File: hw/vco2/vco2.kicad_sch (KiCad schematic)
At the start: 51 parts, among them U4 TL072HxD, U5 TL072HxD

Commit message: Dual VCO board
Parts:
- removed H2, H3, H4: MountingHole, MountingHole:MountingHole_3.5mm, symbol Mechanical:MountingHole
- added C19, C20, C22, C23: 100n, Capacitor_SMD:C_0603_1608Metric_Pad1.08x0.95mm_HandSolder, symbol Device:C
- added C21: 100n, Capacitor_SMD:C_0805_2012Metric_Pad1.18x1.45mm_HandSolder, symbol Device:C
- added D3, D4: LED wave out, LED_THT:LED_D3.0mm, symbol Device:LED
- added J_CV2, J_PULSE2, J_PWM2, J_SAW2, J_TRI2: TS, Connector_Audio:Jack_3.5mm_QingPu_WQP-PJ398SM_Vertical_CircularHoles, symbol Connector_Audio:AudioJack2_SwitchT
- added R39, R44, R52, R53, R54, R55: 10k, Resistor_SMD:R_0603_1608Metric_Pad0.98x0.95mm_HandSolder, symbol Device:R
- added R40: 20k, Resistor_SMD:R_0603_1608Metric_Pad0.98x0.95mm_HandSolder, symbol Device:R
- added R41, R60, R61, R62: 1k, Resistor_SMD:R_0603_1608Metric_Pad0.98x0.95mm_HandSolder, symbol Device:R
- added R42, R43, R46, R49, R50: 49k9, Resistor_SMD:R_0603_1608Metric_Pad0.98x0.95mm_HandSolder, symbol Device:R
- added R45: 250k, Resistor_SMD:R_0603_1608Metric_Pad0.98x0.95mm_HandSolder, symbol Device:R
- added R51: 32k, Resistor_SMD:R_0603_1608Metric_Pad0.98x0.95mm_HandSolder, symbol Device:R
- added R56, R57, R58, R59: 39k, Resistor_SMD:R_0603_1608Metric_Pad0.98x0.95mm_HandSolder, symbol Device:R
- added RV_PWM2, RV_RANGE2, RV_TUNE2: 20k, Pot:RV9012NO, symbol Device:R_Potentiometer
- added TP7: TestPoint_Alt, Holes:TP_0.9mm, symbol Connector:TestPoint_Alt
- added U7, U8: TL072HxD, Package_SO:SOIC-8_3.9x4.9mm_P1.27mm, symbol Amplifier_Operational:TL072
- H1: footprint MountingHole:MountingHole_3.5mm -> MountingHole:MountingHole_3.2mm_M3_Pad
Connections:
- net +12V: now also C19.1, C22.1, U7.8 (V+), U8.8 (V+)
- net +2V5: now also R39.2, R40.2, R51.2, RV_TUNE2.3
- net -12V: now also C20.2, C23.2, U7.4 (V-), U8.4 (V-)
- net GND: now also C19.2, C20.1, C22.2, C23.1, D3.1 (K), D4.2 (A), J_CV2.S, J_PULSE2.S, J_PWM2.S, J_SAW2.S, J_TRI2.S, R41.1, R49.1, RV_RANGE2.1, RV_TUNE2.1
- net OPREF: now also U7.3 (+), U7.5 (+), U8.3 (+), U8.5 (+)
- net at J_CV1.T, R14.1: now also J_CV2.TN
- net EXPO_FREQ renamed EXPO_FREQ1
- net HARD_SYNC renamed HARD_SYNC1
- net LIN_FREQ renamed LIN_FREQ1
- net PULSE_OUT renamed PULSE1
- net PWM_CTRL renamed PWM_CTRL1
- net SAW_OUT renamed SAW1
- net TRI_OUT renamed TRI1
- new net: D3.2 (A), D4.1 (K), R62.2
- new net: R59.1, R62.1, U8.7
- new net: J_TRI2.T, R61.1
- new net: R58.1, R61.2, U8.1
- new net: R55.1, R59.2, U8.6 (-)
- new net: R54.1, R58.2, U8.2 (-)
- new net: R44.1, RV_RANGE2.2
- new net: R39.1, RV_RANGE2.3
- new net: R56.1, R60.2, U7.1
- new net: R52.1, R56.2, U7.2 (-)
- new net: C21.2, J_PULSE2.T
- new net: R53.1, R57.2, U7.6 (-)
- new net: J_CV2.T, R46.1
- new net: R45.1, RV_TUNE2.2
- new net: R43.2, R49.2, R50.1
- new net: C21.1, R57.1, U7.7
- new net: J_PWM2.T, R43.1
- new net: R40.1, RV_PWM2.1
- new net: R42.1, RV_PWM2.2
- new net: R41.2, RV_PWM2.3
- new net: J_SAW2.T, R60.1
- new net EXPO_FREQ2: R44.2, R45.2, R46.2, R51.1, TP7.1
- new net PULSE2: R53.2
- new net PWM_CTRL2: R42.2, R50.2
- new net SAW2: R52.2
- new net TRI2: R54.2, R55.2
- no-connect marks 3 -> 6
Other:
- added sheet Oscillator 2 (osc1.kicad_sch)
- sheet Oscillator 1 ports: added EXPO_FREQ, HARD_SYNC, LIN_FREQ, PULSE, PWM_CTRL, SAW, TRI; removed none
- note added: "INPUT 1"
- note added: "INPUT 2"
- note added: "OUTPUT 1"
- note added: "OUTPUT 2"
- moved on the sheet: C10, C11, C12, C14, C15, C16, C9, D1, D2, J_CV1, J_FM1, J_PULSE1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

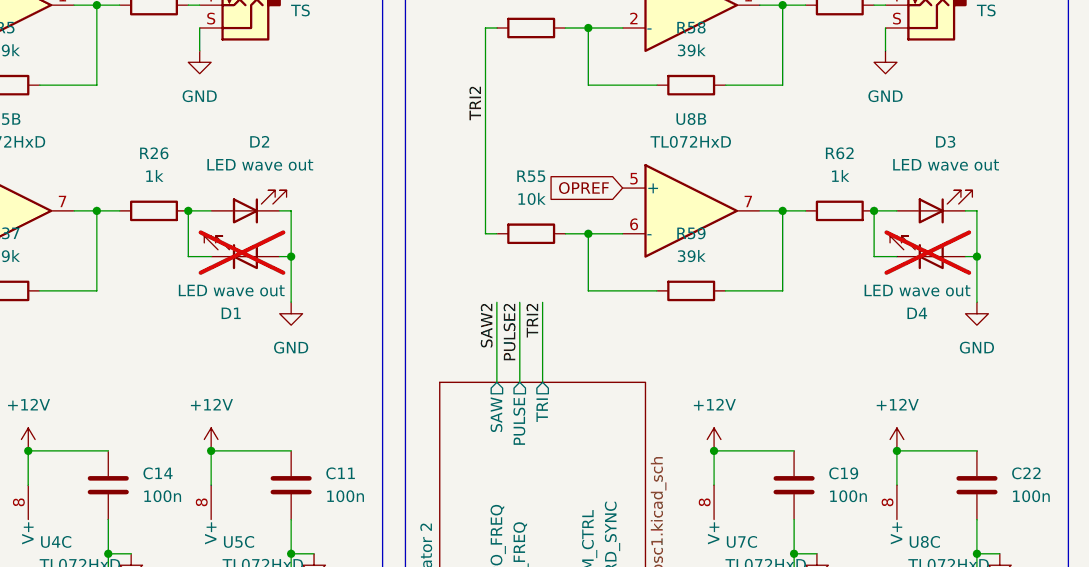
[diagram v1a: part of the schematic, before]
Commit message: Layout VCO2 board
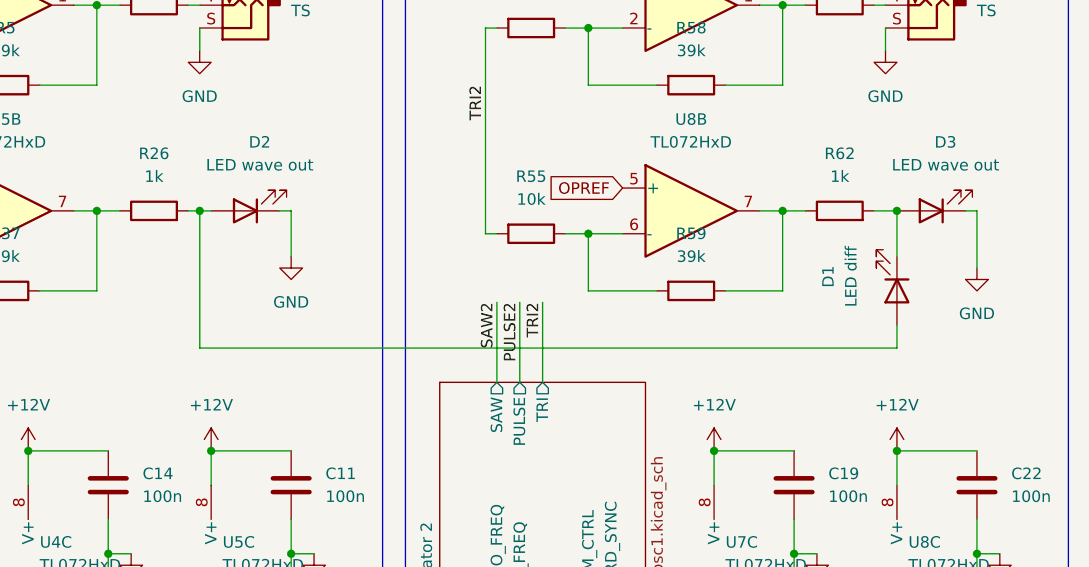
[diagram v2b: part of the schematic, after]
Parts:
- removed D4: LED wave out, LED_THT:LED_D3.0mm, symbol Device:LED
- D1: value LED wave out -> LED diff; now fitted
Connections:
- net GND: no longer D1.2 (A)
- net at D3.2 (A), R62.2: now also D1.1 (K)
- net at D2.2 (A), R26.2: now also D1.2 (A); no longer D1.1 (K)

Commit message: Place components
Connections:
- no-connect marks 6 -> 12
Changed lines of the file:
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@@
+	)
+	(no_connect
+		(at 261.62 29.21)
+	)
+	(no_connect
+		(at 185.42 29.21)
 	)
 	(no_connect
 		(at 31.75 102.87)
+	)
+	(no_connect
+		(at 185.42 53.34)
 	)
 	(no_connect
@@
 	)
 	(no_connect
+		(at 185.42 76.2)
+	)
+	(no_connect
 		(at 90.17 179.07)
+	)
+	(no_connect
+		(at 261.62 76.2)
 	)
 	(no_connect
@@
 	)
 	(no_connect
+		(at 261.62 53.34)
+	)
+	(no_connect

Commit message: Layout board
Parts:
- added H2, H3: MountingHole, Holes:MountingHole_3.2mm_M3_Pad, symbol Mechanical:MountingHole
- H1: footprint MountingHole:MountingHole_3.2mm_M3_Pad -> Holes:MountingHole_3.2mm_M3_Pad
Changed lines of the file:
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@@
 			)
 		)
-		(property "Footprint" "MountingHole:MountingHole_3.2mm_M3_Pad"
+		(property "Footprint" "Holes:MountingHole_3.2mm_M3_Pad"
 			(at 160.02 180.34 0)
 			(effects
@@
 	)
 	(symbol
+		(lib_id "Mechanical:MountingHole")
+		(at 160.02 170.18 0)
+		(unit 1)
+		(exclude_from_sim no)
+		(in_bom no)
+		(on_board yes)
+		(dnp no)
+		(fields_autoplaced yes)
+		(property "Reference" "H3"
+			(at 162.56 168.9099 0)
+			(effects
+				(font
+					(size 1.27 1.27)
+				)
+				(justify left)
+			)
+		)
+		(property "Value" "MountingHole"
+			(at 162.56 171.4499 0)
+			(effects
+				(font
+					(size 1.27 1.27)
+				)
+				(justify left)
+			)
+		)
+		(property "Footprint" "Holes:MountingHole_3.2mm_M3_Pad"
+			(at 160.02 170.18 0)
+			(effects
+				(font
+					(size 1.27 1.27)
+				)
+				(hide yes)
+			)
+		)
+		(property "Datasheet" "~"
+			(at 160.02 170.18 0)
+			(effects
+				(font
+					(size 1.27 1.27)
+				)
+				(hide yes)
+			)
+		)
+		(property "Description" "Mounting Hole without connection"
+			(at 160.02 170.18 0)
+			(effects
+				(font
+					(size 1.27 1.27)
+				)
+				(hide yes)
+			)
+		)
+		(instances
+			(project "vco2"
+				(path "/307302bf-1f04-498b-81c7-0944a093f10d"
+					(reference "H3")
+					(unit 1)
+				)
+			)
+		)
+	)
+	(symbol
 		(lib_id "Device:R")
 		(at 104.14 34.29 90)
@@
 					(unit 1)
 				)
+			)
+		)
+	)
+	(symbol
+		(lib_id "Mechanical:MountingHole")
+		(at 160.02 175.26 0)
+		(unit 1)
+		(exclude_from_sim no)
+		(in_bom no)
+		(on_board yes)
+		(dnp no)
+		(fields_autoplaced yes)
+		(property "Reference" "H2"
+			(at 162.56 173.9899 0)
+			(effects
+				(font
+					(size 1.27 1.27)
+				)
+				(justify left)
+			)
+		)
+		(property "Value" "MountingHole"
+			(at 162.56 176.5299 0)
+			(effects
+				(font
+					(size 1.27 1.27)
+				)
+				(justify left)
+			)
+		)
+		(property "Footprint" "Holes:MountingHole_3.2mm_M3_Pad"
+			(at 160.02 175.26 0)
+			(effects
+				(font
+					(size 1.27 1.27)
+				)
+				(hide yes)
+			)
+		)
+		(property "Datasheet" "~"
+			(at 160.02 175.26 0)
+			(effects
+				(font
+					(size 1.27 1.27)
+				)
+				(hide yes)
+			)
+		)
+		(property "Description" "Mounting Hole without connection"
+			(at 160.02 175.26 0)
+			(effects
+				(font
+					(size 1.27 1.27)
+				)
+				(hide yes)
+			)
+		)
+		(instances
+			(project "vco2"
+				(path "/307302bf-1f04-498b-81c7-0944a093f10d"
+					(reference "H2")
+					(unit 1)
+				)

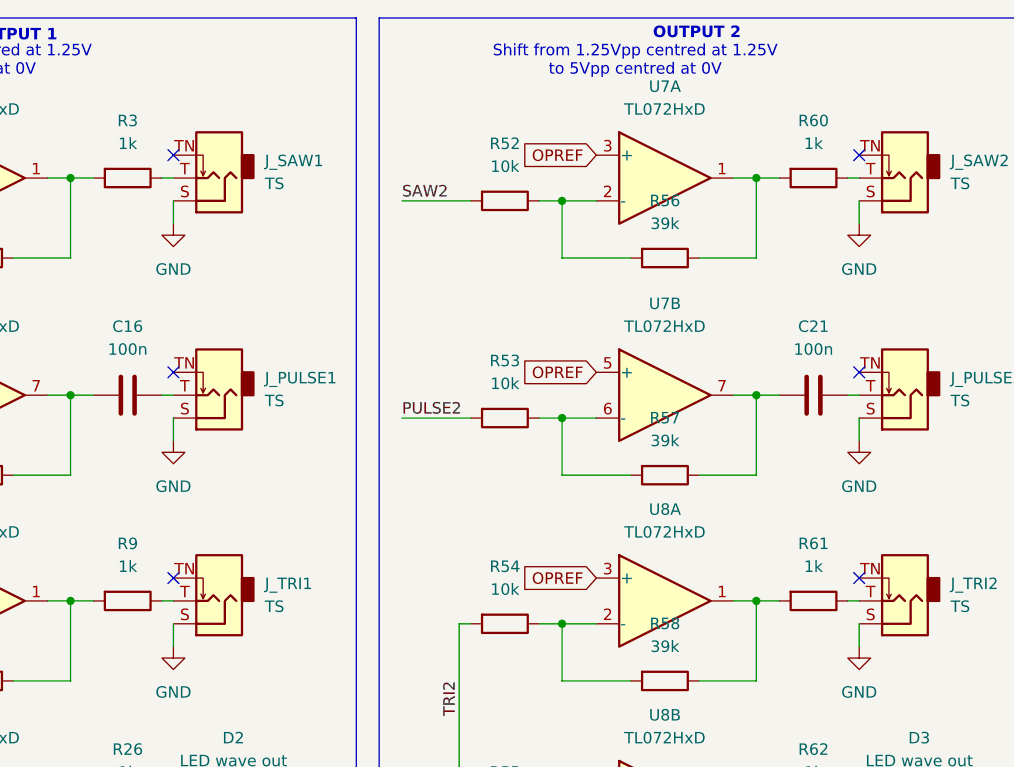
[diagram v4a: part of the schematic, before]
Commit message: Add normalisation on outputs
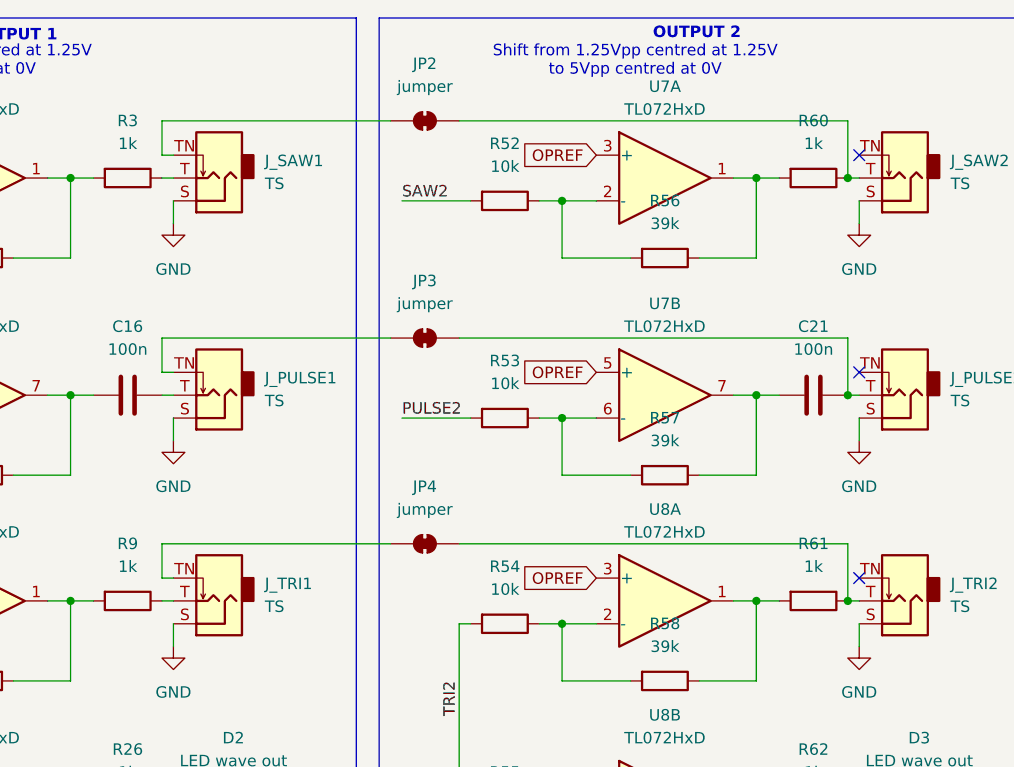
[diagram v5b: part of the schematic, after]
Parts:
- added JP2, JP4: jumper, Jumper:SolderJumper-2_P1.3mm_Bridged2Bar_Pad1.0x1.5mm, symbol Jumper:SolderJumper_2_Bridged
- added JP3: jumper, Jumper:SolderJumper-2_P1.3mm_Open_Pad1.0x1.5mm, symbol Jumper:SolderJumper_2_Bridged
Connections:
- net at J_TRI2.T, R61.1: now also JP4.1 (A)
- net at J_TRI1.TN: now also JP4.2 (B)
- net at C21.2, J_PULSE2.T: now also JP3.1 (A)
- net at J_SAW2.T, R60.1: now also JP2.1 (A)
- net at J_SAW1.TN: now also JP2.2 (B)
- net at J_PULSE1.TN: now also JP3.2 (B)
- no-connect marks 12 -> 9

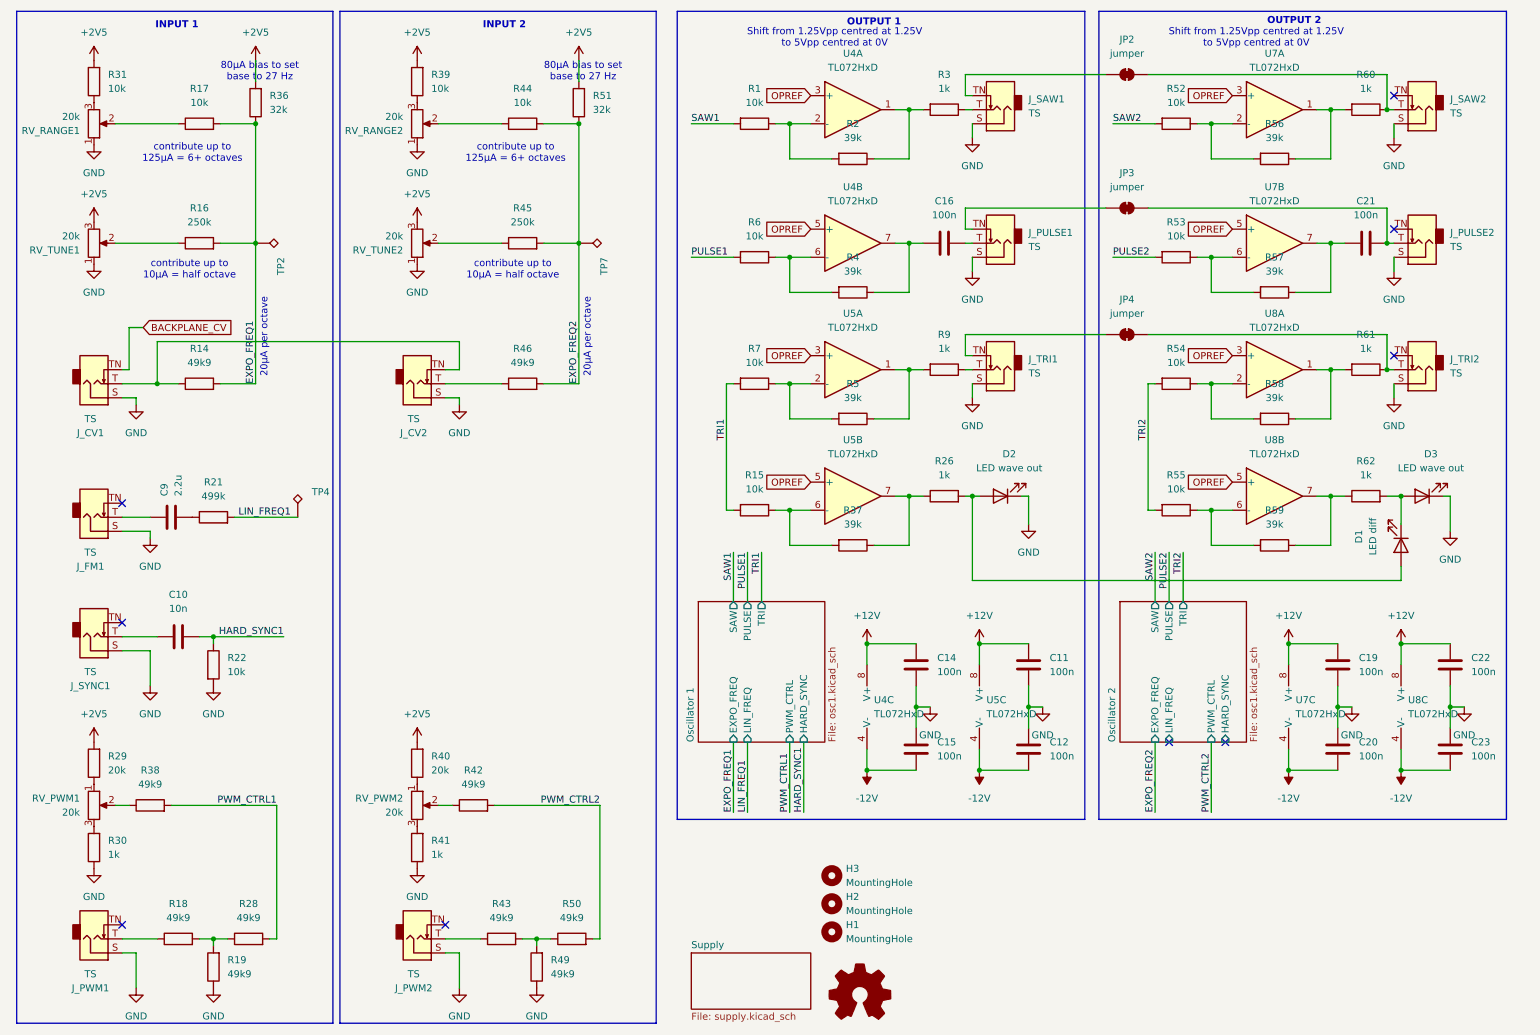
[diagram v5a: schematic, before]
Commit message: WIP: Redesign VCO2 board
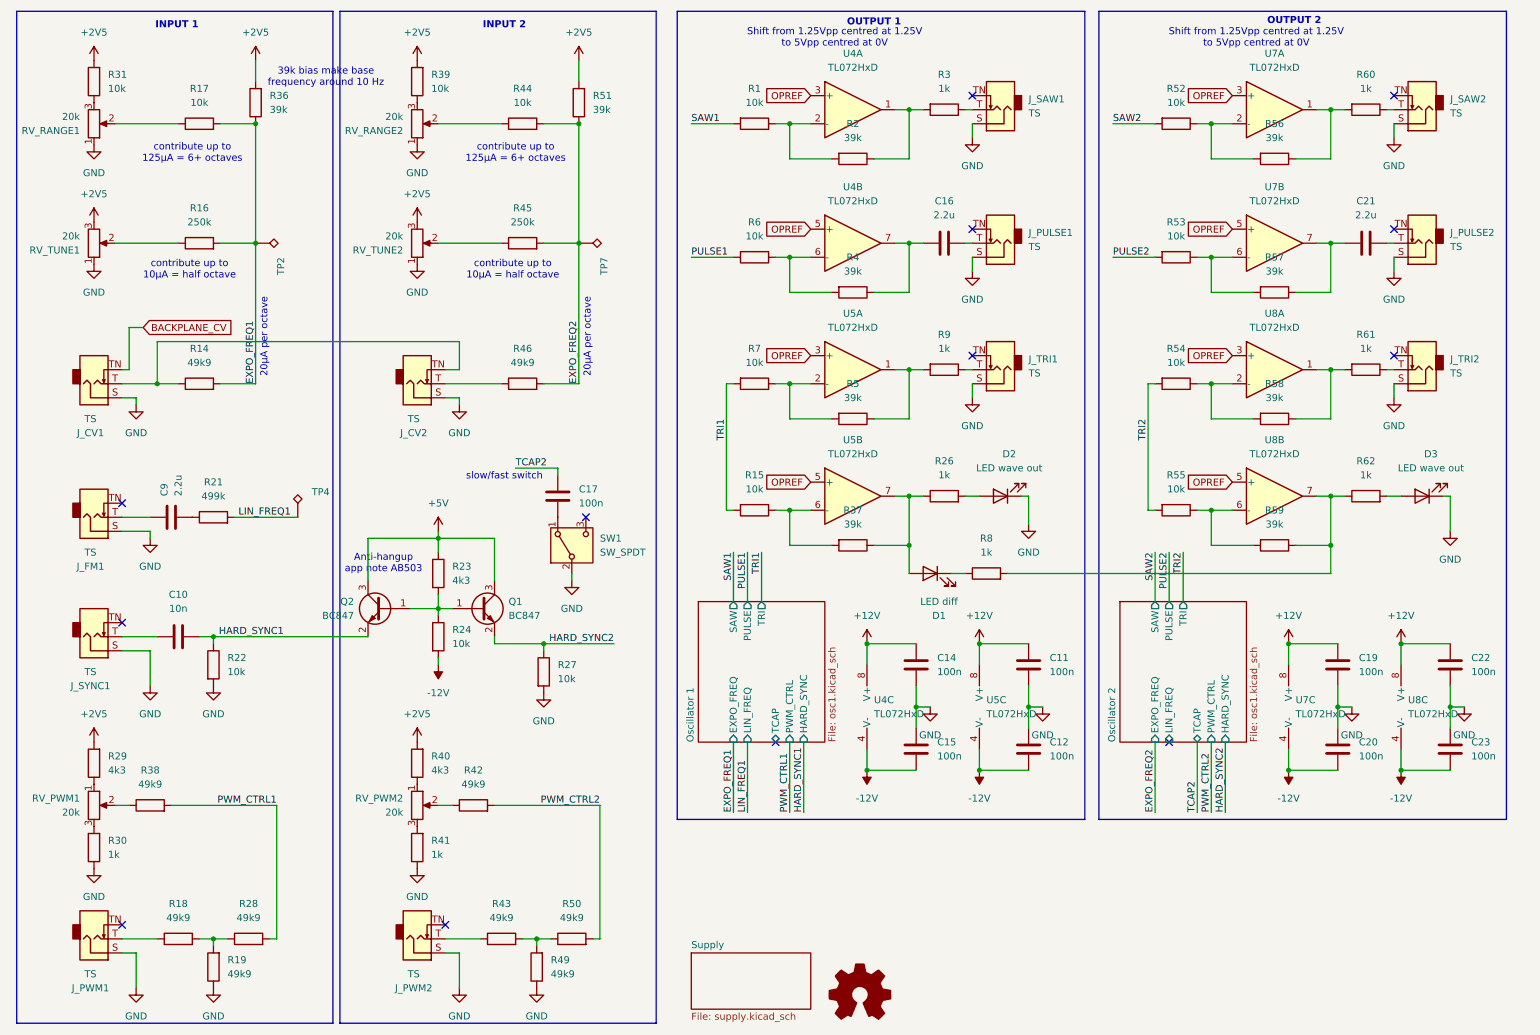
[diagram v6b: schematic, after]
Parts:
- removed H1, H2, H3: MountingHole, Holes:MountingHole_3.2mm_M3_Pad, symbol Mechanical:MountingHole
- removed JP2, JP4: jumper, Jumper:SolderJumper-2_P1.3mm_Bridged2Bar_Pad1.0x1.5mm, symbol Jumper:SolderJumper_2_Bridged
- removed JP3: jumper, Jumper:SolderJumper-2_P1.3mm_Open_Pad1.0x1.5mm, symbol Jumper:SolderJumper_2_Bridged
- added C17: 100n, Capacitor_SMD:C_0603_1608Metric, symbol Device:C
- added Q1, Q2: BC847, Package_TO_SOT_SMD:SOT-23, symbol Transistor_BJT:BC847
- added R23: 4k3, Resistor_SMD:R_0603_1608Metric, symbol Device:R
- added R24, R27: 10k, Resistor_SMD:R_0603_1608Metric, symbol Device:R
- added R8: 1k, Resistor_SMD:R_0603_1608Metric, symbol Device:R
- added SW1: SW_SPDT, Switch:SPDT big pads, symbol Switch:SW_SPDT
- C10, C11, C12, C14, C15, C19, C20, C22, C23: footprint Capacitor_SMD:C_0603_1608Metric_Pad1.08x0.95mm_HandSolder -> Capacitor_SMD:C_0603_1608Metric
- C16, C21: value 100n -> 2.2u; footprint Capacitor_SMD:C_0805_2012Metric_Pad1.18x1.45mm_HandSolder -> Capacitor_SMD:C_0805_2012Metric
- C9: footprint Capacitor_SMD:C_0805_2012Metric_Pad1.18x1.45mm_HandSolder -> Capacitor_SMD:C_0805_2012Metric
- J_CV1, J_CV2, J_FM1, J_PULSE1, J_PULSE2, J_PWM1, J_PWM2, J_SAW1, J_SAW2, J_SYNC1, J_TRI1, J_TRI2: footprint Connector_Audio:Jack_3.5mm_QingPu_WQP-PJ398SM_Vertical_CircularHoles -> Eurorack:Jack_3.5mm_PJ398SM
- R1, R14, R15, R16, R17, R18, R19, R2, R21, R22, R26, R28, R3, R30, R31, R37, R38, R39, R4, R41, R42, R43, R44, R45, R46, R49, R5, R50, R52, R53, R54, R55, R56, R57, R58, R59, R6, R60, R61, R62, R7, R9: footprint Resistor_SMD:R_0603_1608Metric_Pad0.98x0.95mm_HandSolder -> Resistor_SMD:R_0603_1608Metric
- R29, R40: value 20k -> 4k3; footprint Resistor_SMD:R_0603_1608Metric_Pad0.98x0.95mm_HandSolder -> Resistor_SMD:R_0603_1608Metric
- R36, R51: value 32k -> 39k; footprint Resistor_SMD:R_0603_1608Metric_Pad0.98x0.95mm_HandSolder -> Resistor_SMD:R_0603_1608Metric
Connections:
- net -12V: now also R24.2
- net GND: now also R27.2, SW1.2 (B)
- net HARD_SYNC1: now also Q2.2 (E)
- net at D3.2 (A), R62.2: no longer D1.1 (K)
- net at R59.1, R62.1, U8.7: now also R8.2
- net at R26.1, R37.1, U5.7: now also D1.2 (A)
- net at D2.2 (A), R26.2: no longer D1.2 (A)
- new net: Q1.1 (B), Q2.1 (B), R23.2, R24.1
- new net: C17.2, SW1.1 (A)
- new net: D1.1 (K), R8.1
- new net +5V: Q1.3 (C), Q2.3 (C), R23.1
- new net HARD_SYNC2: Q1.2 (E), R27.1
- new net TCAP2: C17.1
- no-connect marks 9 -> 13
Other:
- sheet Oscillator 1 ports: added TCAP; removed none
- sheet Oscillator 2 ports: added TCAP; removed none
- note added: "39k bias make base frequency around 10 Hz"
- note added: "Anti-hangup app note AB503"
- note added: "slow/fast switch"
- note removed: "80µA bias to set base to 27 Hz"
- moved on the sheet: D1
